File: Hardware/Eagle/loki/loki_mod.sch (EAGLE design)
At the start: 39 parts

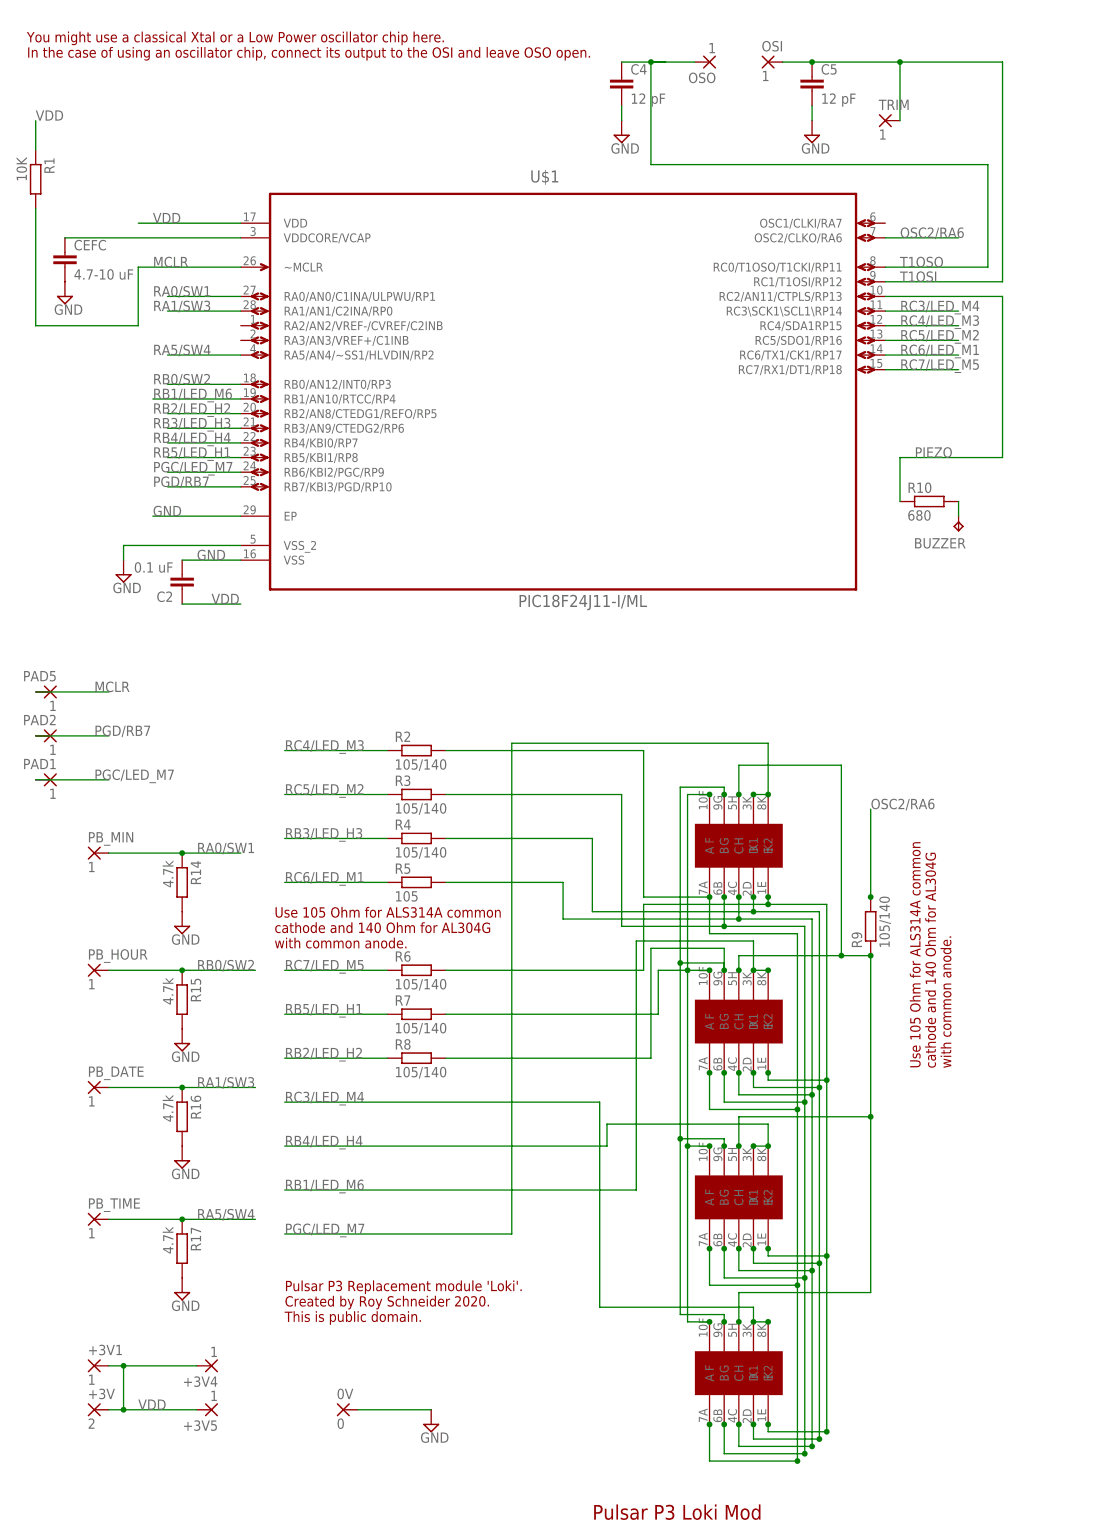
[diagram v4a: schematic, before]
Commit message: Reworked layout for odin and loki boards.
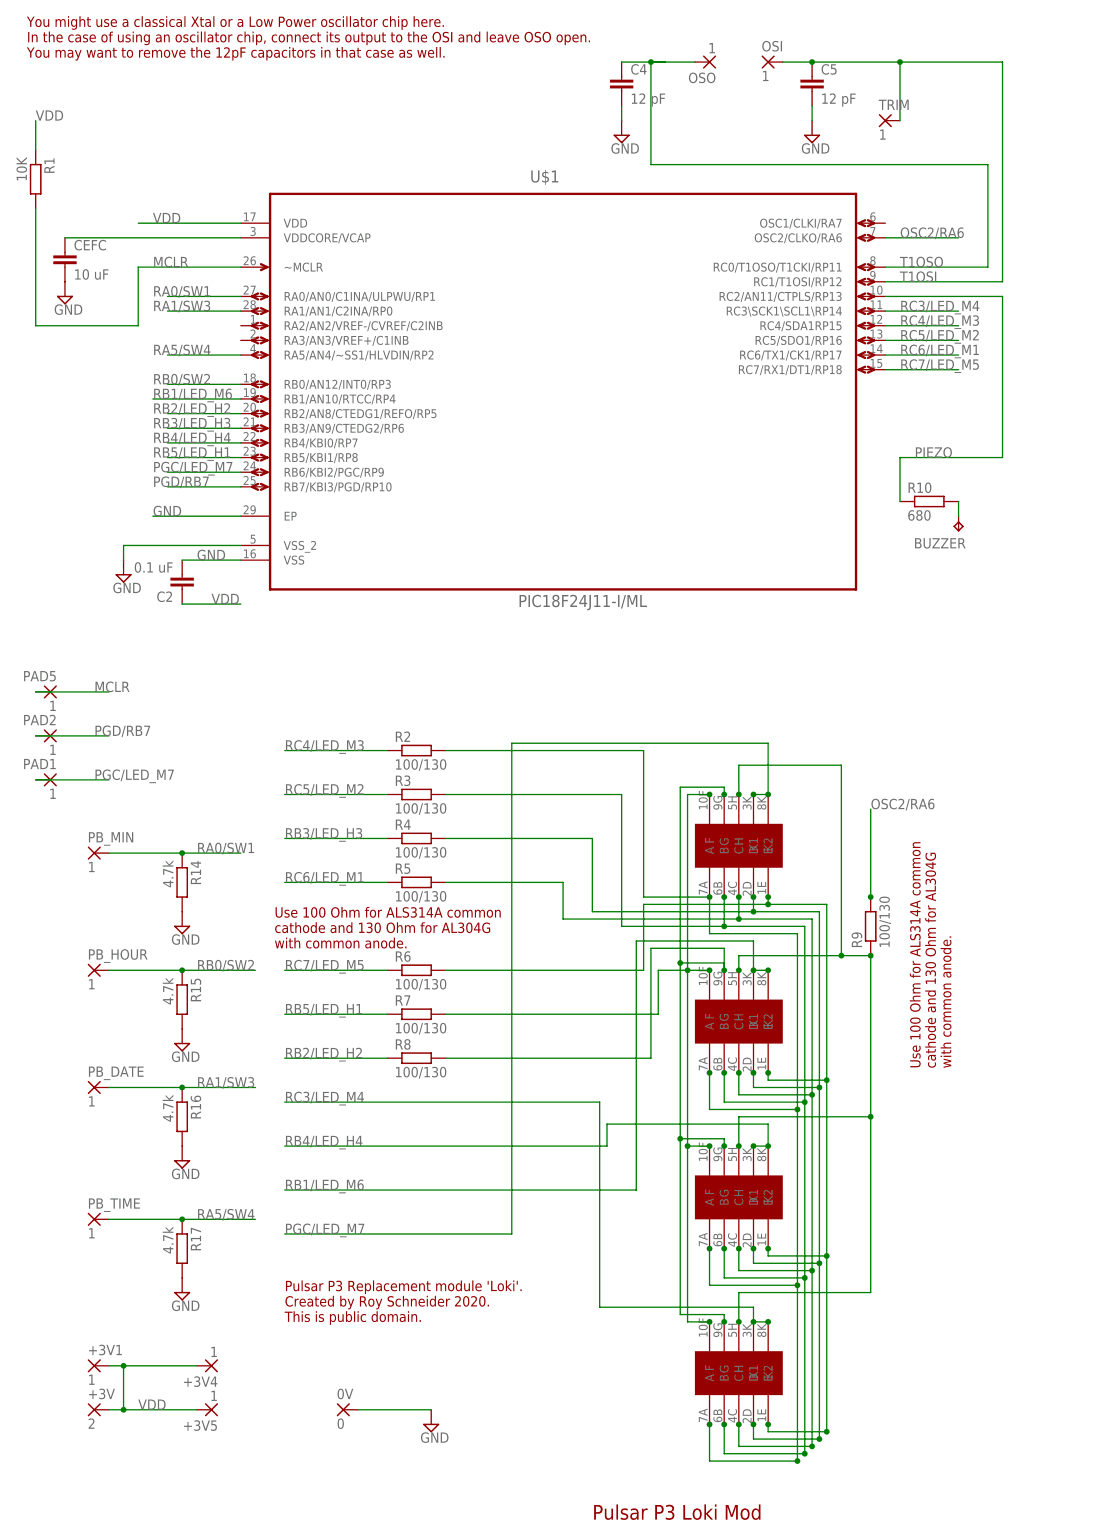
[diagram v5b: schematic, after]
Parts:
- CEFC: value 4.7-10 uF -> 10 uF
- R2, R3, R4, R6, R7, R8, R9: value 105/140 -> 100/130
- R5: value 105 -> 100/130
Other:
- note added: "Use 100 Ohm for ALS314A common cathode and 130 Ohm for AL304G with common anode."
- note added: "You might use a classical Xtal or a Low Power oscillator chip here. In the case of using an oscillator chip, connect its output to the OSI and leave OSO open. You may want to remove the 12pF capacitors in that case as well."
- note removed: "Use 105 Ohm for ALS314A common cathode and 140 Ohm for AL304G with common anode."
- note removed: "You might use a classical Xtal or a Low Power oscillator chip here. In the case of using an oscillator chip, connect its output to the OSI and leave OSO open."
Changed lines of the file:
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@@
 <part name="R1" library="rcl" deviceset="R-EU_" device="R0402" value="10K"/>
 <part name="C2" library="resistor" deviceset="C-EU" device="C0603" value="0.1 uF"/>
-<part name="CEFC" library="resistor" deviceset="C-EU" device="C0603" value="4.7-10 uF"/>
+<part name="CEFC" library="resistor" deviceset="C-EU" device="C0603" value="10 uF"/>
 <part name="SUPPLY2" library="supply2" deviceset="GND" device=""/>
 <part name="SUPPLY3" library="supply2" deviceset="GND" device=""/>
-<part name="R2" library="resistor" deviceset="R-EU_" device="R0402" value="105/140"/>
-<part name="R3" library="resistor" deviceset="R-EU_" device="R0402" value="105/140"/>
-<part name="R4" library="resistor" deviceset="R-EU_" device="R0402" value="105/140"/>
-<part name="R5" library="resistor" deviceset="R-EU_" device="R0402" value="105"/>
-<part name="R6" library="resistor" deviceset="R-EU_" device="R0402" value="105/140"/>
-<part name="R7" library="resistor" deviceset="R-EU_" device="R0402" value="105/140"/>
-<part name="R8" library="resistor" deviceset="R-EU_" device="R0402" value="105/140"/>
+<part name="R2" library="resistor" deviceset="R-EU_" device="R0402" value="100/130"/>
+<part name="R3" library="resistor" deviceset="R-EU_" device="R0402" value="100/130"/>
+<part name="R4" library="resistor" deviceset="R-EU_" device="R0402" value="100/130"/>
+<part name="R5" library="resistor" deviceset="R-EU_" device="R0402" value="100/130"/>
+<part name="R6" library="resistor" deviceset="R-EU_" device="R0402" value="100/130"/>
+<part name="R7" library="resistor" deviceset="R-EU_" device="R0402" value="100/130"/>
+<part name="R8" library="resistor" deviceset="R-EU_" device="R0402" value="100/130"/>
 <part name="R14" library="resistor" deviceset="R-EU_" device="R0402" value="4.7k"/>
 <part name="R15" library="resistor" deviceset="R-EU_" device="R0402" value="4.7k"/>
@@
 <part name="10M" library="l104g" deviceset="L104G" device=""/>
 <part name="1M" library="l104g" deviceset="L104G" device=""/>
-<part name="R9" library="resistor" deviceset="R-EU_" device="R0402" value="105/140"/>
+<part name="R9" library="resistor" deviceset="R-EU_" device="R0402" value="100/130"/>
 <part name="R10" library="resistor" deviceset="R-EU_" device="R0402" value="680"/>
 <part name="BUZZER" library="testpad" deviceset="TP" device="TP06SQ"/>
@@
 <plain>
 <text x="-120.904" y="143.002" size="1.778" layer="94">You might use a classical Xtal or a Low Power oscillator chip here.
-In the case of using an oscillator chip, connect its output to the OSI and leave OSO open.</text>
+In the case of using an oscillator chip, connect its output to the OSI and leave OSO open.
+You may want to remove the 12pF capacitors in that case as well.</text>
 <text x="-76.2" y="-76.2" size="1.778" layer="94">Pulsar P3 Replacement module 'Loki'.
 Created by Roy Schneider 2020.
 This is public domain.</text>
 <text x="-22.86" y="-110.49" size="2.54" layer="94" font="vector">Pulsar P3 Loki Mod</text>
-<text x="-77.978" y="-11.43" size="1.778" layer="94">Use 105 Ohm for ALS314A common
-cathode and 140 Ohm for AL304G
+<text x="-77.978" y="-11.43" size="1.778" layer="94">Use 100 Ohm for ALS314A common
+cathode and 130 Ohm for AL304G
 with common anode.</text>
-<text x="39.37" y="-32.258" size="1.778" layer="94" rot="R90">Use 105 Ohm for ALS314A common
-cathode and 140 Ohm for AL304G
+<text x="39.37" y="-32.258" size="1.778" layer="94" rot="R90">Use 100 Ohm for ALS314A common
+cathode and 130 Ohm for AL304G
 with common anode.</text>
 </plain>
